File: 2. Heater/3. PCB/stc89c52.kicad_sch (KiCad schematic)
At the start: 38 parts, among them IC1 STC89C52rc, J1 USB-Type-C, K1 relay, Q1 S8050, SW1 3x4, SW2 up, SW3 down, SW4 switch, SW5 ctrl, U1 ADC0832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

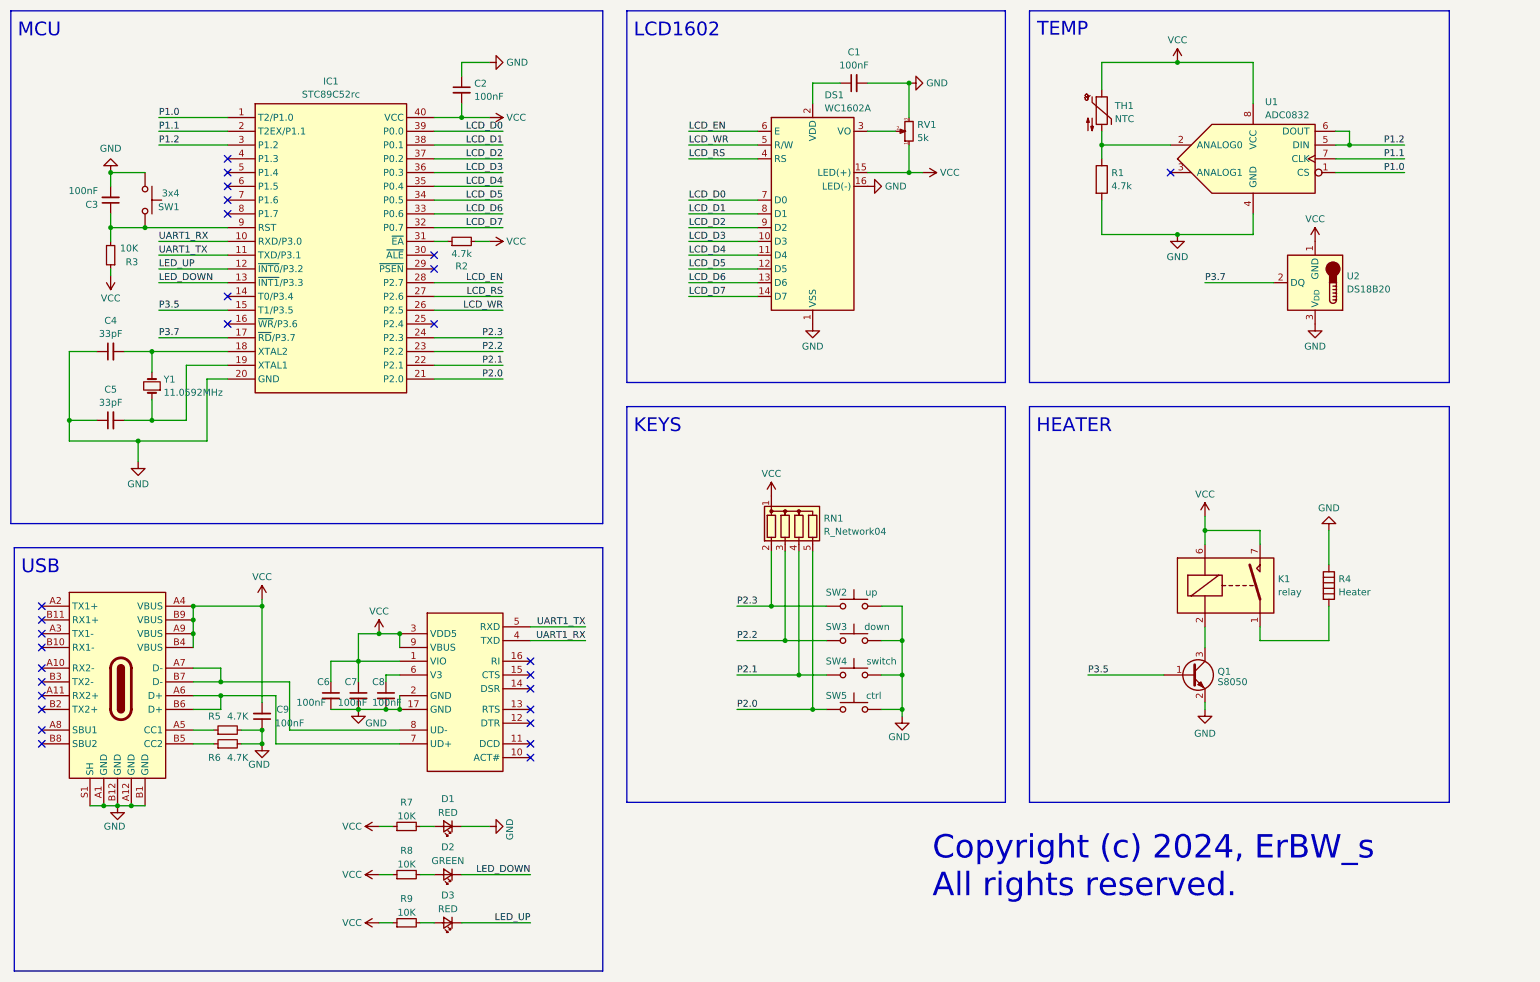
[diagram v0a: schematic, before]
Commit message: add 24v conn
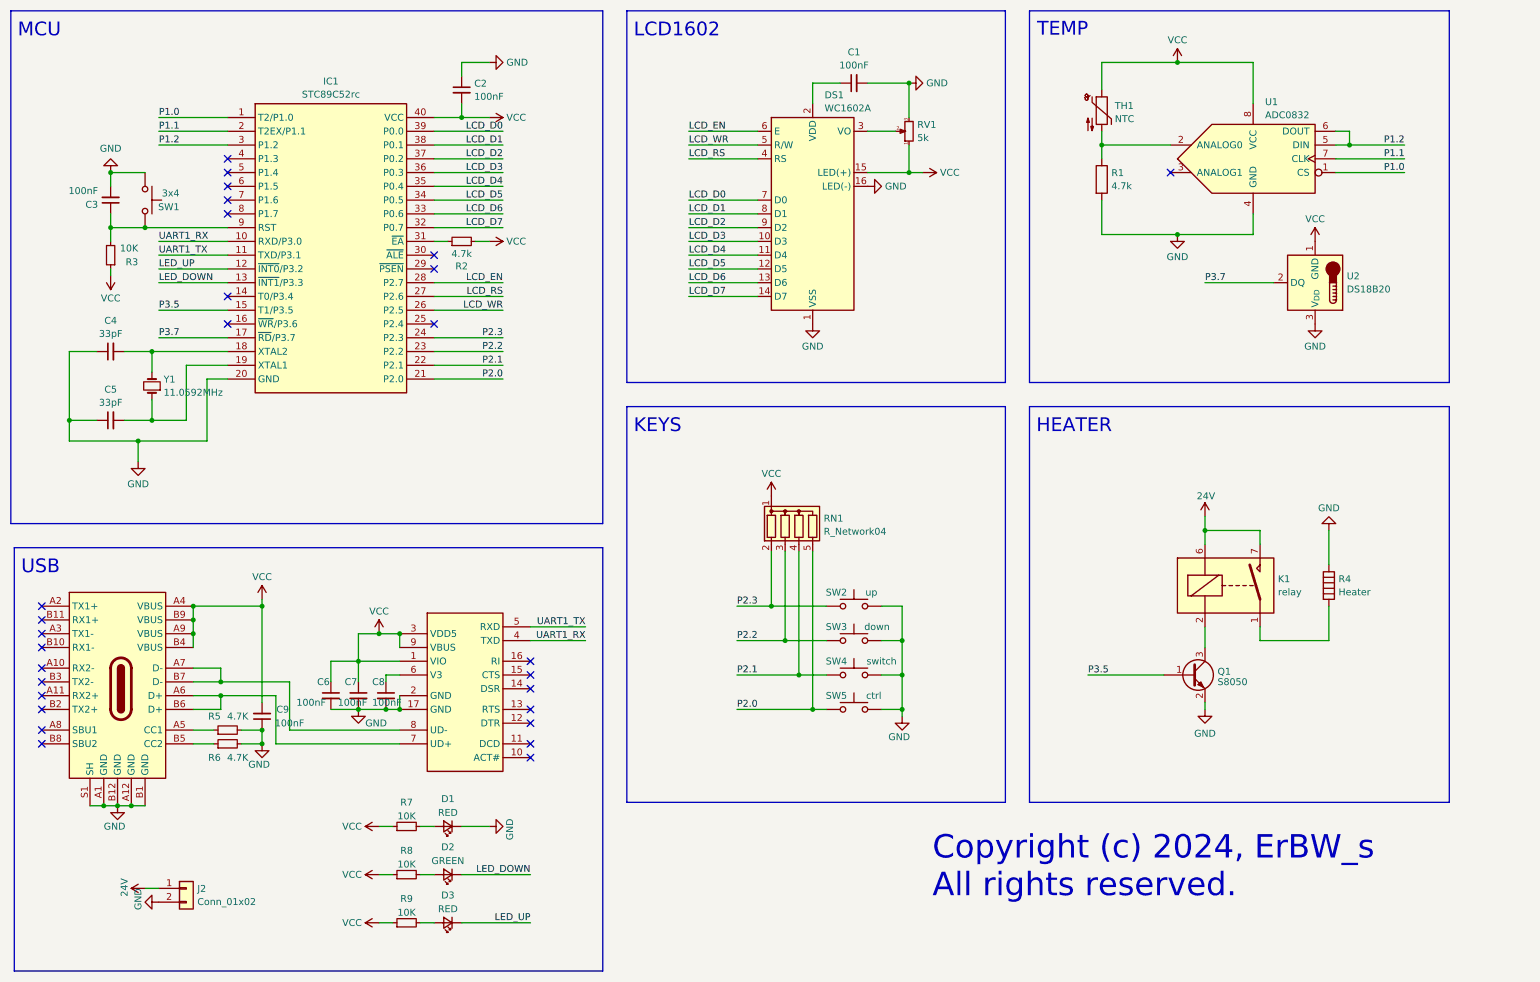
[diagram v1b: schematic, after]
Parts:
- added J2: Conn_01x02, ErBW_s:VCC_CONN, symbol Connector_Generic:Conn_01x02
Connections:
- net GND: now also J2.2 (Pin_2)
- net VCC: no longer K1.6, K1.7, K1.8
- new net 24V: J2.1 (Pin_1), K1.6, K1.7, K1.8
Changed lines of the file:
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@@
 	(wire
 		(pts
+			(xy 40.64 177.8) (xy 43.18 177.8)
+		)
+		(stroke
+			(width 0)
+			(type default)
+		)
+	)
+	(wire
+		(pts
 			(xy 43.18 71.12) (xy 55.88 71.12)
 		)
@@
 	)
 	(symbol
+		(lib_id "power:GND")
+		(at 43.18 180.34 270)
+		(unit 1)
+		(exclude_from_sim no)
+		(in_bom yes)
+		(on_board yes)
+		(dnp no)
+		(property "Reference" "#PWR029"
+			(at 36.83 180.34 0)
+			(effects
+				(font
+					(size 1.27 1.27)
+				)
+				(hide yes)
+			)
+		)
+		(property "Value" "GND"
+			(at 39.37 177.8 0)
+			(effects
+				(font
+					(size 1.27 1.27)
+				)
+				(justify left)
+			)
+		)
+		(property "Footprint" ""
+			(at 43.18 180.34 0)
+			(effects
+				(font
+					(size 1.27 1.27)
+				)
+				(hide yes)
+			)
+		)
+		(property "Datasheet" ""
+			(at 43.18 180.34 0)
+			(effects
+				(font
+					(size 1.27 1.27)
+				)
+				(hide yes)
+			)
+		)
+		(property "Description" ""
+			(at 43.18 180.34 0)
+			(effects
+				(font
+					(size 1.27 1.27)
+				)
+				(hide yes)
+			)
+		)
+		(pin "1"
+		)
+		(instances
+			(project "stc89c52"
+				(path "/92400dd8-8423-466d-ac9e-a05fa9e40883"
+					(reference "#PWR029")
+					(unit 1)
+				)
+			)
+		)
+	)
+	(symbol
 		(lib_id "power:VCC")
 		(at 184.15 45.72 270)
@@
 	)
 	(symbol
+		(lib_id "Connector_Generic:Conn_01x02")
+		(at 48.26 177.8 0)
+		(unit 1)
+		(exclude_from_sim no)
+		(in_bom yes)
+		(on_board yes)
+		(dnp no)
+		(fields_autoplaced yes)
+		(property "Reference" "J2"
+			(at 50.292 177.8578 0)
+			(effects
+				(font
+					(size 1.27 1.27)
+				)
+				(justify left)
+			)
+		)
+		(property "Value" "Conn_01x02"
+			(at 50.292 180.2821 0)
+			(effects
+				(font
+					(size 1.27 1.27)
+				)
+				(justify left)
+			)
+		)
+		(property "Footprint" "ErBW_s:VCC_CONN"
+			(at 48.26 177.8 0)
+			(effects
+				(font
+					(size 1.27 1.27)
+				)
+				(hide yes)
+			)
+		)
+		(property "Datasheet" "~"
+			(at 48.26 177.8 0)
+			(effects
+				(font
+					(size 1.27 1.27)
+				)
+				(hide yes)
+			)
+		)
+		(property "Description" "Generic connector, single row, 01x02, script generated (kicad-library-utils/schlib/autogen/connector/)"
+			(at 48.26 177.8 0)
+			(effects
+				(font
+					(size 1.27 1.27)
+				)
+				(hide yes)
+			)
+		)
+		(pin "1"
+		)
+		(pin "2"
+		)
+		(instances
+			(project ""
+				(path "/92400dd8-8423-466d-ac9e-a05fa9e40883"
+					(reference "J2")
+					(unit 1)
+				)
+			)
+		)
+	)
+	(symbol
 		(lib_id "power:VCC")
 		(at 83.82 175.26 90)
@@
 	)
 	(symbol
+		(lib_id "power:VCC")
+		(at 40.64 177.8 90)
+		(unit 1)
+		(exclude_from_sim no)
+		(in_bom yes)
+		(on_board yes)
+		(dnp no)
+		(property "Reference" "#PWR028"
+			(at 44.45 177.8 0)
+			(effects
+				(font
+					(size 1.27 1.27)
+				)
+				(hide yes)
+			)
+		)
+		(property "Value" "24V"
+			(at 36.83 179.324 0)
+			(effects
+				(font
+					(size 1.27 1.27)
+				)
+				(justify left)
+			)
+		)
+		(property "Footprint" ""
+			(at 40.64 177.8 0)
+			(effects
+				(font
+					(size 1.27 1.27)
+				)
+				(hide yes)
+			)
+		)
+		(property "Datasheet" ""
+			(at 40.64 177.8 0)
+			(effects
+				(font
+					(size 1.27 1.27)
+				)
+				(hide yes)
+			)
+		)
+		(property "Description" "Power symbol creates a global label with name \"VCC\""
+			(at 40.64 177.8 0)
+			(effects
+				(font
+					(size 1.27 1.27)
+				)
+				(hide yes)
+			)
+		)
+		(pin "1"
+		)
+		(instances
+			(project "stc89c52"
+				(path "/92400dd8-8423-466d-ac9e-a05fa9e40883"
+					(reference "#PWR028")
+					(unit 1)
+				)
+			)
+		)
+	)
+	(symbol
 		(lib_id "Switch:SW_Push")
 		(at 171.45 125.73 0)
@@
 		(on_board yes)
 		(dnp no)
-		(fields_autoplaced yes)
 		(property "Reference" "#PWR016"
 			(at 236.22 113.03 0)
@@
 			)
 		)
-		(property "Value" "VCC"
-			(at 236.22 105.0869 0)
+		(property "Value" "24V"
+			(at 234.696 105.41 0)
 			(effects
 				(font
 					(size 1.27 1.27)
 				)
+				(justify left)
 			)
 		)
